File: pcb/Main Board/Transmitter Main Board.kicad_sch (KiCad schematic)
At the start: 12 parts, among them J1 Battery, J2 BATTERY MONITOR, J3 Throttle, J4 Steering, J5 VR3, J6 XY JOYSTICK, U1 Teensy4.1, U2 TLV73312PDBV, U3 NRF24L01_Breakout

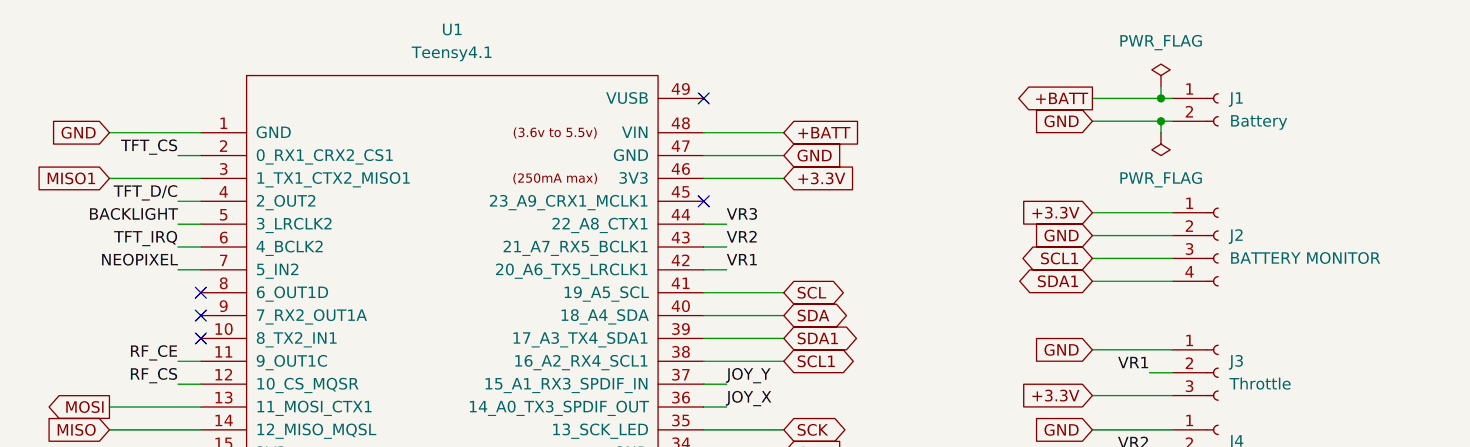
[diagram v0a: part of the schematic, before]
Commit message: Create 4960 symbol and footprint
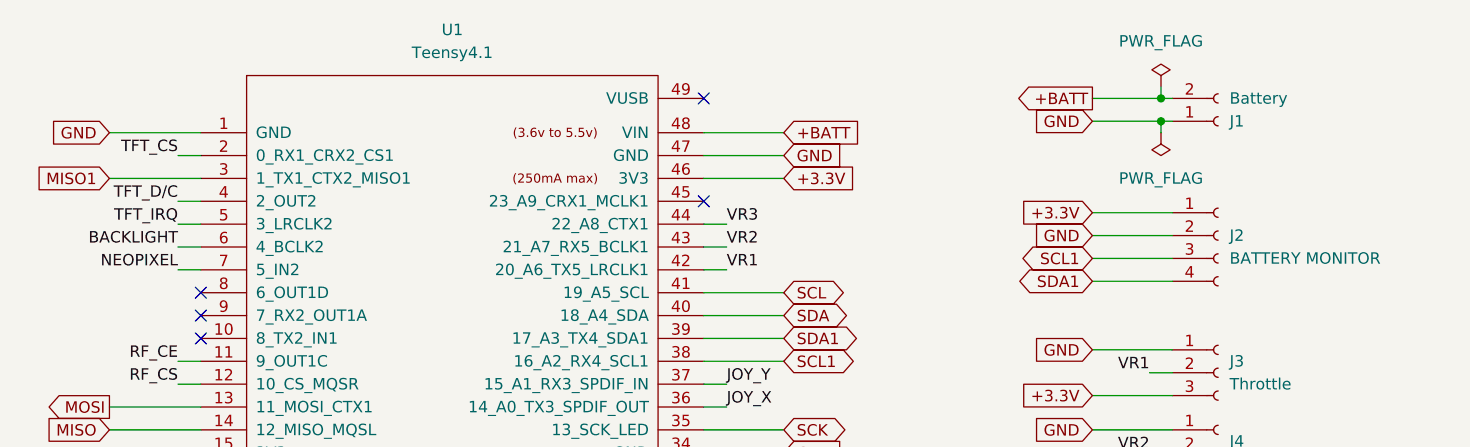
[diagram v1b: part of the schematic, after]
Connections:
- net +BATT: now also J1.2 (Pin_2); no longer J1.1 (Pin_1)
- net BACKLIGHT: now also U1.6 (4_BCLK2); no longer U1.5 (3_LRCLK2)
- net GND: now also J1.1 (Pin_1); no longer J1.2 (Pin_2)
- net TFT_IRQ: now also U1.5 (3_LRCLK2); no longer U1.6 (4_BCLK2)
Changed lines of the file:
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@@
 	)
 	(label "BACKLIGHT"
-		(at 30.48 38.1 180)
+		(at 30.48 40.64 180)
 		(effects
 			(font
@@
 	)
 	(label "TFT_IRQ"
-		(at 30.48 40.64 180)
+		(at 30.48 38.1 180)
 		(effects
 			(font
@@
 	(symbol
 		(lib_id "Connector:Conn_01x02_Socket")
-		(at 146.05 24.13 0)
+		(at 146.05 26.67 0)
+		(mirror x)
 		(unit 1)
 		(exclude_from_sim no)
@@
 		(on_board yes)
 		(dnp no)
-		(fields_autoplaced yes)
 		(property "Reference" "J1"
-			(at 147.32 24.1299 0)
+			(at 147.32 26.6701 0)
 			(effects
 				(font
@@
 		)
 		(property "Value" "Battery"
-			(at 147.32 26.6699 0)
+			(at 147.32 24.1301 0)
 			(effects
 				(font
@@
 		)
 		(property "Footprint" "Connector_JST:JST_PH_B2B-PH-K_1x02_P2.00mm_Vertical"
-			(at 146.05 24.13 0)
+			(at 146.05 26.67 0)
 			(effects
 				(font
@@
 		)
 		(property "Datasheet" "~"
-			(at 146.05 24.13 0)
+			(at 146.05 26.67 0)
 			(effects
 				(font
@@
 		)
 		(property "Description" "Generic connector, single row, 01x02, script generated"
-			(at 146.05 24.13 0)
-			(effects
-				(font
+			(at 146.05 26.67 0)
+			(effects
+				(font

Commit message: more routing
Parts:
- added J7: Neopixel Out, Connector_JST:JST_PH_B3B-PH-K_1x03_P2.00mm_Vertical, symbol Connector:Conn_01x03_Socket
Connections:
- net +3.3V: now also J3.1 (Pin_1), J4.1 (Pin_1), J5.1 (Pin_1), J6.1 (Pin_1), J7.1 (Pin_1); no longer J3.3 (Pin_3), J4.3 (Pin_3), J5.3 (Pin_3), J6.4 (Pin_4)
- net +BATT: no longer LCD1.22 (VIN)
- net 2x8 Button Matrix/NEO_OUT: now also J7.2 (Pin_2)
- net COL_B: now also U1.25 (33_MCLK2); no longer U1.27 (35_TX8)
- net GND: now also J2.4 (Pin_4), J3.3 (Pin_3), J4.3 (Pin_3), J5.3 (Pin_3), J6.4 (Pin_4), J7.3 (Pin_3); no longer J2.2 (Pin_2), J3.1 (Pin_1), J4.1 (Pin_1), J5.1 (Pin_1), J6.1 (Pin_1)
- net ROW_1: now also U1.20 (28_RX7); no longer U1.22 (30_CRX3)
- net ROW_2: now also U1.21 (29_TX7); no longer U1.23 (31_CTX3)
- net ROW_3: now also U1.22 (30_CRX3); no longer U1.24 (32_OUT1B)
- net ROW_4: now also U1.23 (31_CTX3); no longer U1.25 (33_MCLK2)
- net SCL: now also U1.40 (18_A4_SDA); no longer U1.41 (19_A5_SCL)
- net SCL1: now also J2.2 (Pin_2); no longer J2.3 (Pin_3)
- net SDA: now also U1.41 (19_A5_SCL); no longer U1.40 (18_A4_SDA)
- net SDA1: now also J2.3 (Pin_3); no longer J2.4 (Pin_4)
- net VR1: now also U1.44 (22_A8_CTX1); no longer U1.42 (20_A6_TX5_LRCLK1)
- net VR3: now also U1.42 (20_A6_TX5_LRCLK1); no longer U1.44 (22_A8_CTX1)

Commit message: more more more routing
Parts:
- added J3: i2c, Connector_JST:JST_PH_B4B-PH-K_1x04_P2.00mm_Vertical, symbol Connector:Conn_01x04_Socket
- renumbered J3 to J4, J4 to J5, J5 to J6, J6 to J7, J7 to J8
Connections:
- net +3.3V: now also J3.1 (Pin_1)
- net +BATT: now also J1.1 (Pin_1); no longer J1.2 (Pin_2)
- net BACKLIGHT: now also U1.5 (3_LRCLK2); no longer U1.6 (4_BCLK2)
- net GND: now also J1.2 (Pin_2), J3.4 (Pin_4); no longer J1.1 (Pin_1)
- net NEOPIXEL: now also U1.8 (6_OUT1D); no longer U1.7 (5_IN2)
- net ROW_1: now also U1.7 (5_IN2); no longer U1.20 (28_RX7)
- net ROW_2: now also U1.9 (7_RX2_OUT1A); no longer U1.21 (29_TX7)
- net SCL1: now also J3.2 (Pin_2)
- net SDA1: now also J3.3 (Pin_3)
- net TFT_D/C: now also U1.6 (4_BCLK2); no longer U1.4 (2_OUT2)
- net TFT_IRQ: now also U1.4 (2_OUT2); no longer U1.5 (3_LRCLK2)
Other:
- moved on the sheet: J4, J5, J6, J7

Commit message: finalish routing
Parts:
- added J8: UART6/i2c2, Connector_JST:JST_PH_B4B-PH-K_1x04_P2.00mm_Vertical, symbol Connector:Conn_01x04_Socket
- added J9: UART7, Connector_JST:JST_PH_B4B-PH-K_1x04_P2.00mm_Vertical, symbol Connector:Conn_01x04_Socket
- renumbered J8 to J10, J7 to J4, J6 to J5, J5 to J6, J4 to J7
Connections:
- net GND: now also J8.4 (Pin_4), J9.4 (Pin_4)
- net RF_PWR: now reaches C2.1, U2.5 (OUT), U3.2 (VCC)
- net 3V3: now reaches U1.15 (3V3)
- net 3V3: now also J8.1 (Pin_1), J9.1 (Pin_1)
- net TX6: now reaches U1.16 (24_A10_TX6_SCL2)
- net TX6: now also J8.2 (Pin_2)
- net RX6: now reaches U1.17 (25_A11_RX6_SDA2)
- net RX6: now also J8.3 (Pin_3)
- net RX7: now reaches U1.20 (28_RX7)
- net RX7: now also J9.3 (Pin_3)
- net TX7: now reaches U1.21 (29_TX7)
- net TX7: now also J9.2 (Pin_2)
- no-connect marks 59 -> 54
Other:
- moved on the sheet: J4, J5, J6, J7

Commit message: Final final routing
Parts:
- added H1, H2: MountingHole_Pad, MountingHole:MountingHole_3.2mm_M3_Pad, symbol Mechanical:MountingHole_Pad
- added JP1, JP2, JP3: SolderJumper_3_Bridged12, Jumper:SolderJumper-3_P2.0mm_Open_TrianglePad1.0x1.5mm, symbol Jumper:SolderJumper_3_Open
- J3: value i2c -> UART4/i2c1
- J4: renamed from J5; value VR3 -> Aux IO; footprint Connector_JST:JST_PH_B3B-PH-K_1x03_P2.00mm_Vertical -> Connector_JST:JST_PH_B4B-PH-K_1x04_P2.00mm_Vertical; symbol Connector:Conn_01x03_Socket -> Connector:Conn_01x04_Socket
- J7: renamed from J4; value XY JOYSTICK -> XY Joystick/UART3; footprint Connector_JST:JST_PH_B4B-PH-K_1x04_P2.00mm_Vertical -> Connector_JST:JST_PH_B5B-PH-K_1x05_P2.00mm_Vertical; symbol Connector:Conn_01x04_Socket -> Connector:Conn_01x05_Socket
- J8, J9: footprint Connector_JST:JST_PH_B4B-PH-K_1x04_P2.00mm_Vertical -> Connector_JST:JST_PH_B5B-PH-K_1x05_P2.00mm_Vertical; symbol Connector:Conn_01x04_Socket -> Connector:Conn_01x05_Socket
- renumbered J6 to J5, J7 to J6
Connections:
- net +3.3V: no longer J7.1 (Pin_1)
- net +BATT: now also JP1.3 (B), JP2.3 (B), JP3.3 (B)
- net 3V3: now also JP1.1 (A), JP2.1 (A), JP3.1 (A); no longer J8.1 (Pin_1), J9.1 (Pin_1)
- net GND: now also J4.4 (Pin_4), J7.5 (Pin_5), J8.5 (Pin_5), J9.5 (Pin_5), H1.1, H2.1; no longer J4.3 (Pin_3), J7.4 (Pin_4), J8.4 (Pin_4), J9.4 (Pin_4)
- net JOY_X: now also J7.3 (Pin_3), U1.32 (40_A16); no longer J7.2 (Pin_2), U1.36 (14_A0_TX3_SPDIF_OUT)
- net JOY_Y: now also J7.4 (Pin_4), U1.33 (41_A17); no longer J7.3 (Pin_3), U1.37 (15_A1_RX3_SPDIF_IN)
- net RF_CE: now also U1.36 (14_A0_TX3_SPDIF_OUT); no longer U1.11 (9_OUT1C)
- net RF_EN: now also U1.37 (15_A1_RX3_SPDIF_IN); no longer U1.33 (41_A17)
- net RX6: now also J8.4 (Pin_4); no longer J8.3 (Pin_3)
- net RX7: now also J9.4 (Pin_4); no longer J9.3 (Pin_3)
- net SCL: now also U1.41 (19_A5_SCL); no longer U1.40 (18_A4_SDA)
- net SDA: now also U1.40 (18_A4_SDA); no longer U1.41 (19_A5_SCL)
- net TX6: now also J8.3 (Pin_3); no longer J8.2 (Pin_2)
- net TX7: now also J9.3 (Pin_3); no longer J9.2 (Pin_2)
- net VR1: now also U1.45 (23_A9_CRX1_MCLK1); no longer U1.44 (22_A8_CTX1)
- net VR2: now also U1.44 (22_A8_CTX1); no longer U1.43 (21_A7_RX5_BCLK1)
- net VR3: now also J4.3 (Pin_3), U1.43 (21_A7_RX5_BCLK1); no longer J4.2 (Pin_2), U1.42 (20_A6_TX5_LRCLK1)
- net UART7_AUX: now reaches U1.28 (36_CS)
- net UART7_AUX: now also J9.2 (Pin_2)
- net UART6_AUX: now reaches U1.29 (37_CS)
- net UART6_AUX: now also J8.2 (Pin_2)
- net BTN: now reaches U1.31 (39_MISO1_OUT1A)
- net BTN: now also J7.2 (Pin_2)
- new net: J9.1 (Pin_1), JP3.2 (C)
- new net: J8.1 (Pin_1), JP2.2 (C)
- new net: J7.1 (Pin_1), JP1.2 (C)
- new net VR4: J4.2 (Pin_2), U1.42 (20_A6_TX5_LRCLK1)
- no-connect marks 54 -> 50
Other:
- moved on the sheet: C1, C2, J1, J10, J2, J3, J5, J6, LCD1, U1, U2, U3

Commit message: begin overcomplication
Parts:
- removed J2: BATTERY MONITOR, Connector_JST:JST_PH_B4B-PH-K_1x04_P2.00mm_Vertical, symbol Connector:Conn_01x04_Socket
- added JP1: SolderJumper_3_Bridged12, Jumper:SolderJumper-3_P2.0mm_Open_TrianglePad1.0x1.5mm, symbol Jumper:SolderJumper_3_Open
- added R1, R2, R3, R4: R, Resistor_SMD:R_0805_2012Metric_Pad1.20x1.40mm_HandSolder, symbol Device:R
- J2: renamed from J3; footprint Connector_JST:JST_PH_B4B-PH-K_1x04_P2.00mm_Vertical -> Connector_JST:JST_PH_B5B-PH-K_1x05_P2.00mm_Vertical; symbol Connector:Conn_01x04_Socket -> Connector:Conn_01x05_Socket
- renumbered J4 to J3, J5 to J4, J6 to J5, J7 to J6, J8 to J7, J9 to J8, J10 to J9, JP1 to JP2, JP2 to JP3, JP3 to JP4
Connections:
- net +3.3V: now also JP1.1 (A), R1.1, R2.1, R3.2, R4.2; no longer J2.1 (Pin_1)
- net +BATT: now also JP1.3 (B)
- net GND: now also J2.5 (Pin_5); no longer J2.4 (Pin_4)
- net SCL: now also R3.1
- net SCL1: now also J2.3 (Pin_3), R1.2; no longer J2.2 (Pin_2)
- net SDA: now also R4.1
- net SDA1: now also J2.4 (Pin_4), R2.2; no longer J2.3 (Pin_3)
- net i2c1_INT: now reaches U1.10 (8_TX2_IN1)
- net i2c1_INT: now also J2.2 (Pin_2)
- new net: J2.1 (Pin_1), JP1.2 (C)
- no-connect marks 50 -> 49
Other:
- moved on the sheet: J1, J3, J4, J5, J6, J7, J8, JP2, JP3, JP4
